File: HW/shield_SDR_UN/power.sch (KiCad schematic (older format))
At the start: 16 parts

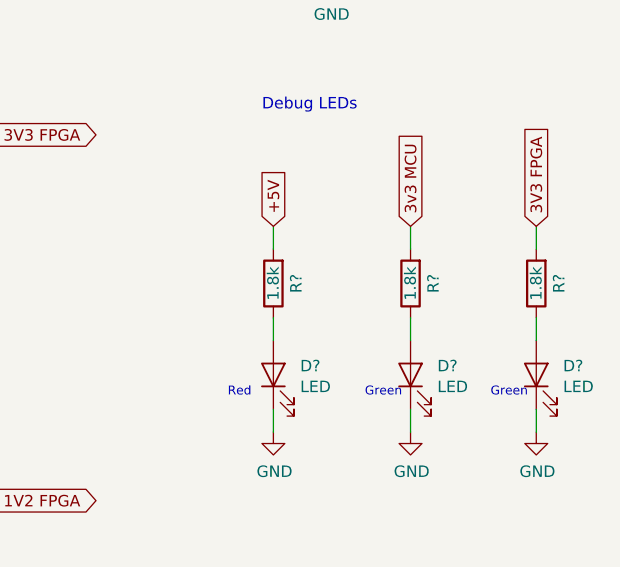
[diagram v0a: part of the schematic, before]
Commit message: Footprints added for C and R
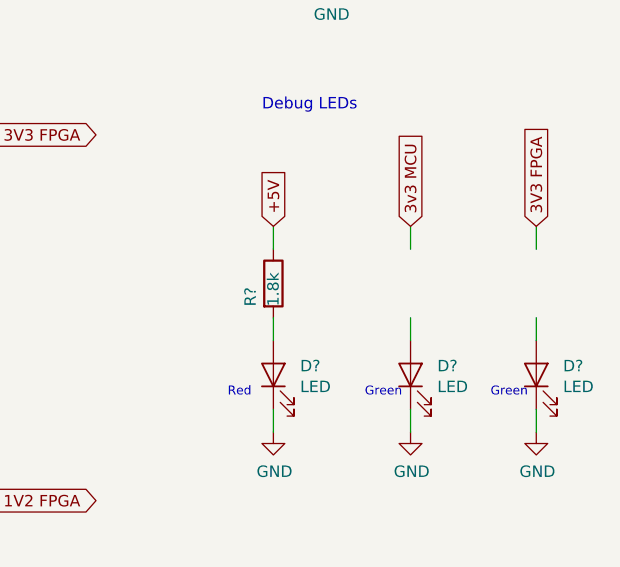
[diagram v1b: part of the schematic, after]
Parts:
- removed C? (x5): 4.7uF, Capacitor_SMD:C_0603_1608Metric_Pad1.05x0.95mm_HandSolder, symbol Device:C
- removed D?: LED, LED_SMD:LED_0805_2012Metric_Pad1.15x1.40mm_HandSolder, symbol Device:LED
- removed R? (x3): 1.8k, Resistor_SMD:R_0603_1608Metric_Pad1.05x0.95mm_HandSolder, symbol Device:R
- added C? (x5): 4.7uF, Capacitor_SMD:C_0603_1608Metric_Pad1.05x0.95mm_HandSolder, symbol Device:C
- added D?: LED, LED_SMD:LED_0805_2012Metric_Pad1.15x1.40mm_HandSolder, symbol Device:LED
- added R?: 1.8k, Resistor_SMD:R_0603_1608Metric_Pad1.05x0.95mm_HandSolder, symbol Device:R
- C?: Digikey (none) -> 1276-1045-1-ND
- D?: footprint LED_SMD:LED_0805_2012Metric_Pad1.15x1.40mm_HandSolder -> LED_SMD:LED_0603_1608Metric_Pad1.05x0.95mm_HandSolder; Digikey (none) -> 160-1469-1-ND
- D?: Digikey (none) -> 160-1468-1-ND
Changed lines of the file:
@@
 Comment4 ""
 $EndDescr
-$Comp
-L Device:C C?
-U 1 1 5CCD952E
-P 1550 3550
-F 0 "C?" H 1665 3596 50  0000 L CNN
-F 1 "4.7uF" H 1665 3505 50  0000 L CNN
-F 2 "Capacitor_SMD:C_0603_1608Metric_Pad1.05x0.95mm_HandSolder" H 1588 3400 50  0001 C CNN
-F 3 "~" H 1550 3550 50  0001 C CNN
-	1    1550 3550
-	1    0    0    -1
-$EndComp
-$Comp
-L Device:C C?
-U 1 1 5CCDBE29
-P 3450 3550
-F 0 "C?" H 3565 3596 50  0000 L CNN
-F 1 "4.7uF" H 3565 3505 50  0000 L CNN
-F 2 "Capacitor_SMD:C_0603_1608Metric_Pad1.05x0.95mm_HandSolder" H 3488 3400 50  0001 C CNN
-F 3 "~" H 3450 3550 50  0001 C CNN
-	1    3450 3550
-	1    0    0    -1
-$EndComp
 Wire Wire Line
 	3850 3300 3450 3300
@@
 Wire Wire Line
 	1550 3850 1550 3700
-$Comp
-L Device:C C?
-U 1 1 5CCEBA00
-P 1550 5150
-F 0 "C?" H 1665 5196 50  0000 L CNN
-F 1 "4.7uF" H 1665 5105 50  0000 L CNN
-F 2 "Capacitor_SMD:C_0603_1608Metric_Pad1.05x0.95mm_HandSolder" H 1588 5000 50  0001 C CNN
-F 3 "~" H 1550 5150 50  0001 C CNN
-	1    1550 5150
-	1    0    0    -1
-$EndComp
 Wire Wire Line
 	3850 4900 3450 4900
@@
 F 1 "4.7uF" H 1665 1955 50  0000 L CNN
 F 2 "Capacitor_SMD:C_0603_1608Metric_Pad1.05x0.95mm_HandSolder" H 1588 1850 50  0001 C CNN
-F 3 "~" H 1550 2000 50  0001 C CNN
+F 3 "www.samsungsem.com/kr/support/product-search/mlcc/CL10A475KQ8NNNC.jsp" H 1550 2000 50  0001 C CNN
+F 4 "1276-1045-1-ND " H 1550 2000 50  0001 C CNN "Digikey"
 	1    1550 2000
-	1    0    0    -1
-$EndComp
-$Comp
-L Device:C C?
-U 1 1 5CD3AA74
-P 3450 2000
-F 0 "C?" H 3565 2046 50  0000 L CNN
-F 1 "4.7uF" H 3565 1955 50  0000 L CNN
-F 2 "Capacitor_SMD:C_0603_1608Metric_Pad1.05x0.95mm_HandSolder" H 3488 1850 50  0001 C CNN
-F 3 "~" H 3450 2000 50  0001 C CNN
-	1    3450 2000
 	1    0    0    -1
 $EndComp
@@
 Text GLabel 1400 3300 0    50   Input ~ 0
 +5V
-$Comp
-L Device:C C?
-U 1 1 5CCEBA0A
-P 3450 5150
-F 0 "C?" H 3565 5196 50  0000 L CNN
-F 1 "4.7uF" H 3565 5105 50  0000 L CNN
-F 2 "Capacitor_SMD:C_0603_1608Metric_Pad1.05x0.95mm_HandSolder" H 3488 5000 50  0001 C CNN
-F 3 "~" H 3450 5150 50  0001 C CNN
-	1    3450 5150
-	1    0    0    -1
-$EndComp
 $Comp
 L power:GND #PWR0187
@@
 Debug LEDs
 $Comp
-L Device:R R?
-U 1 1 5CE70567
-P 5050 3950
-AR Path="/5CC081D2/5CE70567" Ref="R?"  Part="1"
-AR Path="/5CC08321/5CE70567" Ref="R?"  Part="0"
-F 0 "R?" V 4950 3950 50  0000 C CNN
-F 1 "1.8k" V 5050 3950 50  0000 C CNN
-F 2 "Resistor_SMD:R_0603_1608Metric_Pad1.05x0.95mm_HandSolder" V 4980 3950 50  0001 C CNN
-F 3 "~" H 5050 3950 50  0001 C CNN
-	1    5050 3950
-	-1   0    0    1
-$EndComp
-$Comp
 L Device:LED D?
 U 1 1 5CE70571
 P 5050 4350
 AR Path="/5CC081D2/5CE70571" Ref="D?"  Part="1"
-AR Path="/5CC08321/5CE70571" Ref="D?"  Part="0"
+AR Path="/5CC08321/5CE70571" Ref="D?"  Part="1"
 F 0 "D?" V 5089 4233 50  0000 R CNN
 F 1 "LED" V 4998 4233 50  0000 R CNN
-F 2 "LED_SMD:LED_0805_2012Metric_Pad1.15x1.40mm_HandSolder" H 5050 4350 50  0001 C CNN
-F 3 "~" H 5050 4350 50  0001 C CNN
+F 2 "LED_SMD:LED_0603_1608Metric_Pad1.05x0.95mm_HandSolder" H 5050 4350 50  0001 C CNN
+F 3 "optoelectronics.liteon.com/upload/download/DS22-2000-137/LTST-S220KRKT.pdf" H 5050 4350 50  0001 C CNN
+F 4 "160-1469-1-ND" V 5050 4350 50  0001 C CNN "Digikey"
 	1    5050 4350
 	0    -1   -1   0
@@
 Red
 $Comp
-L Device:R R?
-U 1 1 5CE85D9C
-P 5650 3950
-AR Path="/5CC081D2/5CE85D9C" Ref="R?"  Part="1"
-AR Path="/5CC08321/5CE85D9C" Ref="R?"  Part="0"
-F 0 "R?" V 5550 3950 50  0000 C CNN
-F 1 "1.8k" V 5650 3950 50  0000 C CNN
-F 2 "Resistor_SMD:R_0603_1608Metric_Pad1.05x0.95mm_HandSolder" V 5580 3950 50  0001 C CNN
-F 3 "~" H 5650 3950 50  0001 C CNN
-	1    5650 3950
-	-1   0    0    1
-$EndComp
-$Comp
 L Device:LED D?
 U 1 1 5CE85DA6
 P 5650 4350
 AR Path="/5CC081D2/5CE85DA6" Ref="D?"  Part="1"
-AR Path="/5CC08321/5CE85DA6" Ref="D?"  Part="0"
+AR Path="/5CC08321/5CE85DA6" Ref="D?"  Part="1"
 F 0 "D?" V 5689 4233 50  0000 R CNN
 F 1 "LED" V 5598 4233 50  0000 R CNN
 F 2 "LED_SMD:LED_0805_2012Metric_Pad1.15x1.40mm_HandSolder" H 5650 4350 50  0001 C CNN
-F 3 "~" H 5650 4350 50  0001 C CNN
+F 3 "http://optoelectronics.liteon.com/upload/download/DS22-2000-075/LTST-S220KGKT.pdf" H 5650 4350 50  0001 C CNN
+F 4 "160-1468-1-ND" V 5650 4350 50  0001 C CNN "Digikey"
 	1    5650 4350
 	0    -1   -1   0
@@
 Text GLabel 5650 3700 1    50   Input ~ 0
 3v3 MCU
-$Comp
-L Device:R R?
-U 1 1 5CE8EB5C
-P 6200 3950
-AR Path="/5CC081D2/5CE8EB5C" Ref="R?"  Part="1"
-AR Path="/5CC08321/5CE8EB5C" Ref="R?"  Part="0"
-F 0 "R?" V 6100 3950 50  0000 C CNN
-F 1 "1.8k" V 6200 3950 50  0000 C CNN
-F 2 "Resistor_SMD:R_0603_1608Metric_Pad1.05x0.95mm_HandSolder" V 6130 3950 50  0001 C CNN
-F 3 "~" H 6200 3950 50  0001 C CNN
-	1    6200 3950
-	-1   0    0    1
-$EndComp
-$Comp
-L Device:LED D?
-U 1 1 5CE8EB66
-P 6200 4350
-AR Path="/5CC081D2/5CE8EB66" Ref="D?"  Part="1"
-AR Path="/5CC08321/5CE8EB66" Ref="D?"  Part="0"
-F 0 "D?" V 6239 4233 50  0000 R CNN
-F 1 "LED" V 6148 4233 50  0000 R CNN
-F 2 "LED_SMD:LED_0805_2012Metric_Pad1.15x1.40mm_HandSolder" H 6200 4350 50  0001 C CNN
-F 3 "~" H 6200 4350 50  0001 C CNN
-	1    6200 4350
-	0    -1   -1   0
-$EndComp
 Wire Wire Line
 	6200 4600 6200 4500
@@
 	1    0    0    -1
 $EndComp
+$Comp
+L Device:C C?
+U 1 1 5CFF78BF
+P 1550 3550
+F 0 "C?" H 1665 3596 50  0000 L CNN
+F 1 "4.7uF" H 1665 3505 50  0000 L CNN
+F 2 "Capacitor_SMD:C_0603_1608Metric_Pad1.05x0.95mm_HandSolder" H 1588 3400 50  0001 C CNN
+F 3 "www.samsungsem.com/kr/support/product-search/mlcc/CL10A475KQ8NNNC.jsp" H 1550 3550 50  0001 C CNN
+F 4 "1276-1045-1-ND " H 1550 3550 50  0001 C CNN "Digikey"
+	1    1550 3550
+	1    0    0    -1
+$EndComp
+$Comp
+L Device:C C?
+U 1 1 5CFF8436
+P 1550 5150
+F 0 "C?" H 1665 5196 50  0000 L CNN
+F 1 "4.7uF" H 1665 5105 50  0000 L CNN
+F 2 "Capacitor_SMD:C_0603_1608Metric_Pad1.05x0.95mm_HandSolder" H 1588 5000 50  0001 C CNN
+F 3 "www.samsungsem.com/kr/support/product-search/mlcc/CL10A475KQ8NNNC.jsp" H 1550 5150 50  0001 C CNN
+F 4 "1276-1045-1-ND " H 1550 5150 50  0001 C CNN "Digikey"
+	1    1550 5150
+	1    0    0    -1
+$EndComp
+$Comp
+L Device:C C?
+U 1 1 5CFF9817
+P 3450 5150
+F 0 "C?" H 3565 5196 50  0000 L CNN
+F 1 "4.7uF" H 3565 5105 50  0000 L CNN
+F 2 "Capacitor_SMD:C_0603_1608Metric_Pad1.05x0.95mm_HandSolder" H 3488 5000 50  0001 C CNN
+F 3 "www.samsungsem.com/kr/support/product-search/mlcc/CL10A475KQ8NNNC.jsp" H 3450 5150 50  0001 C CNN
+F 4 "1276-1045-1-ND " H 3450 5150 50  0001 C CNN "Digikey"
+	1    3450 5150
+	1    0    0    -1
+$EndComp
+$Comp
+L Device:C C?
+U 1 1 5CFFA74A
+P 3450 3550
+F 0 "C?" H 3565 3596 50  0000 L CNN
+F 1 "4.7uF" H 3565 3505 50  0000 L CNN
+F 2 "Capacitor_SMD:C_0603_1608Metric_Pad1.05x0.95mm_HandSolder" H 3488 3400 50  0001 C CNN
+F 3 "www.samsungsem.com/kr/support/product-search/mlcc/CL10A475KQ8NNNC.jsp" H 3450 3550 50  0001 C CNN
+F 4 "1276-1045-1-ND " H 3450 3550 50  0001 C CNN "Digikey"
+	1    3450 3550
+	1    0    0    -1
+$EndComp
+$Comp
+L Device:C C?
+U 1 1 5CFFC6D1
+P 3450 2000
+F 0 "C?" H 3565 2046 50  0000 L CNN
+F 1 "4.7uF" H 3565 1955 50  0000 L CNN
+F 2 "Capacitor_SMD:C_0603_1608Metric_Pad1.05x0.95mm_HandSolder" H 3488 1850 50  0001 C CNN
+F 3 "www.samsungsem.com/kr/support/product-search/mlcc/CL10A475KQ8NNNC.jsp" H 3450 2000 50  0001 C CNN
+F 4 "1276-1045-1-ND " H 3450 2000 50  0001 C CNN "Digikey"
+	1    3450 2000
+	1    0    0    -1
+$EndComp
+$Comp
+L Device:R R?
+U 1 1 5D0251D4
+P 5050 3950
+F 0 "R?" V 4950 3850 50  0000 L CNN
+F 1 "1.8k" V 5050 3850 50  0000 L CNN
+F 2 "Resistor_SMD:R_0603_1608Metric_Pad1.05x0.95mm_HandSolder" V 4980 3950 50  0001 C CNN
+F 3 "http://www.yageo.com/documents/recent/PYu-RC_Group_51_RoHS_L_10.pdf" H 5050 3950 50  0001 C CNN
+F 4 "311-1.8KGRTR-ND" V 5050 3950 50  0001 C CNN "Digikey"
+	1    5050 3950
+	1    0    0    -1
+$EndComp
+$Comp
+L Device:LED D?
+U 1 1 5D05C7DE
+P 6200 4350
+AR Path="/5CC081D2/5D05C7DE" Ref="D?"  Part="1"
+AR Path="/5CC08321/5D05C7DE" Ref="D?"  Part="1"
+F 0 "D?" V 6239 4233 50  0000 R CNN
+F 1 "LED" V 6148 4233 50  0000 R CNN
+F 2 "LED_SMD:LED_0805_2012Metric_Pad1.15x1.40mm_HandSolder" H 6200 4350 50  0001 C CNN
+F 3 "http://optoelectronics.liteon.com/upload/download/DS22-2000-075/LTST-S220KGKT.pdf" H 6200 4350 50  0001 C CNN
+F 4 "160-1468-1-ND" V 6200 4350 50  0001 C CNN "Digikey"
+	1    6200 4350
+	0    -1   -1   0
+$EndComp
 $EndSCHEMATC

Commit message: Footprints updated
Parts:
- removed R?: 1.8k, Resistor_SMD:R_0603_1608Metric_Pad1.05x0.95mm_HandSolder, symbol Device:R
- added R? (x2): 470, Resistor_SMD:R_0603_1608Metric_Pad1.05x0.95mm_HandSolder, symbol Device:R
- added R?: 1.8k, Resistor_SMD:R_0603_1608Metric_Pad1.05x0.95mm_HandSolder, symbol Device:R
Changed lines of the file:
@@
-$EndComp
-$Comp
-L Device:R R?
-U 1 1 5D0251D4
-P 5050 3950
-F 0 "R?" V 4950 3850 50  0000 L CNN
-F 1 "1.8k" V 5050 3850 50  0000 L CNN
-F 2 "Resistor_SMD:R_0603_1608Metric_Pad1.05x0.95mm_HandSolder" V 4980 3950 50  0001 C CNN
-F 3 "http://www.yageo.com/documents/recent/PYu-RC_Group_51_RoHS_L_10.pdf" H 5050 3950 50  0001 C CNN
-F 4 "311-1.8KGRTR-ND" V 5050 3950 50  0001 C CNN "Digikey"
-	1    5050 3950
-	1    0    0    -1
 $EndComp
 $Comp
@@
 	0    -1   -1   0
 $EndComp
+$Comp
+L Device:R R?
+U 1 1 5CEB8F9A
+P 5650 3950
+F 0 "R?" H 5700 4000 50  0000 L CNN
+F 1 "470" V 5650 3850 50  0000 L CNN
+F 2 "Resistor_SMD:R_0603_1608Metric_Pad1.05x0.95mm_HandSolder" V 5580 3950 50  0001 C CNN
+F 3 "http://www.yageo.com/documents/recent/PYu-RC_Group_51_RoHS_L_10.pdf" H 5650 3950 50  0001 C CNN
+F 4 "311-470GRCT-ND" V 5650 3950 50  0001 C CNN "Digikey"
+	1    5650 3950
+	1    0    0    -1
+$EndComp
+$Comp
+L Device:R R?
+U 1 1 5CEB98F9
+P 6200 3950
+F 0 "R?" H 6250 4000 50  0000 L CNN
+F 1 "470" V 6200 3850 50  0000 L CNN
+F 2 "Resistor_SMD:R_0603_1608Metric_Pad1.05x0.95mm_HandSolder" V 6130 3950 50  0001 C CNN
+F 3 "http://www.yageo.com/documents/recent/PYu-RC_Group_51_RoHS_L_10.pdf" H 6200 3950 50  0001 C CNN
+F 4 "311-470GRCT-ND" V 6200 3950 50  0001 C CNN "Digikey"
+	1    6200 3950
+	1    0    0    -1
+$EndComp
+$Comp
+L Device:R R?
+U 1 1 5CEE7448
+P 5050 3950
+F 0 "R?" H 5100 4000 50  0000 L CNN
+F 1 "1.8k" V 5050 3850 50  0000 L CNN
+F 2 "Resistor_SMD:R_0603_1608Metric_Pad1.05x0.95mm_HandSolder" V 4980 3950 50  0001 C CNN
+F 3 "http://www.yageo.com/documents/recent/PYu-RC_Group_51_RoHS_L_10.pdf" H 5050 3950 50  0001 C CNN
+F 4 "311-1.8KGRTR-ND" V 5050 3950 50  0001 C CNN "Digikey"
+	1    5050 3950
+	1    0    0    -1
+$EndComp
 $EndSCHEMATC

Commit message: RF-Front-end connections
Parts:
- J?: footprint Connector_USB:USB_Micro-B_GCT_USB3076-30-A -> lib:USB_Micro_B_Female_10118194-0001LF; Digikey (none) -> 609-4618-1-ND
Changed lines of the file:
@@
 F 0 "J?" H 5407 2417 50  0000 C CNN
 F 1 "USB_B_Micro" H 5407 2326 50  0000 C CNN
-F 2 "Connector_USB:USB_Micro-B_GCT_USB3076-30-A" H 5500 1900 50  0001 C CNN
-F 3 "~" H 5500 1900 50  0001 C CNN
+F 2 "lib:USB_Micro_B_Female_10118194-0001LF" H 5500 1900 50  0001 C CNN
+F 3 "https://cdn.amphenol-icc.com/media/wysiwyg/files/documentation/datasheet/inputoutput/io_usb_micro.pdf" H 5500 1900 50  0001 C CNN
+F 4 "609-4618-1-ND" H 5350 1950 50  0001 C CNN "Digikey"
 	1    5350 1950
 	1    0    0    -1

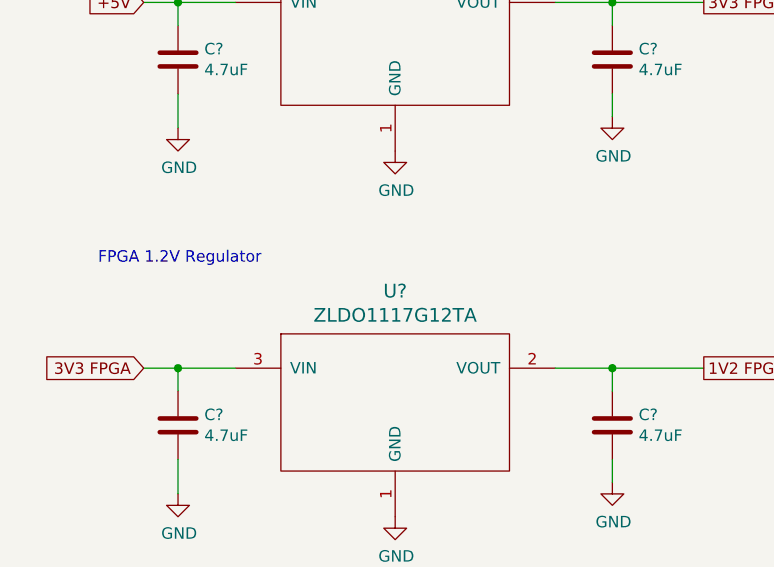
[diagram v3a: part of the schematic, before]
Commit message: JTAG routed
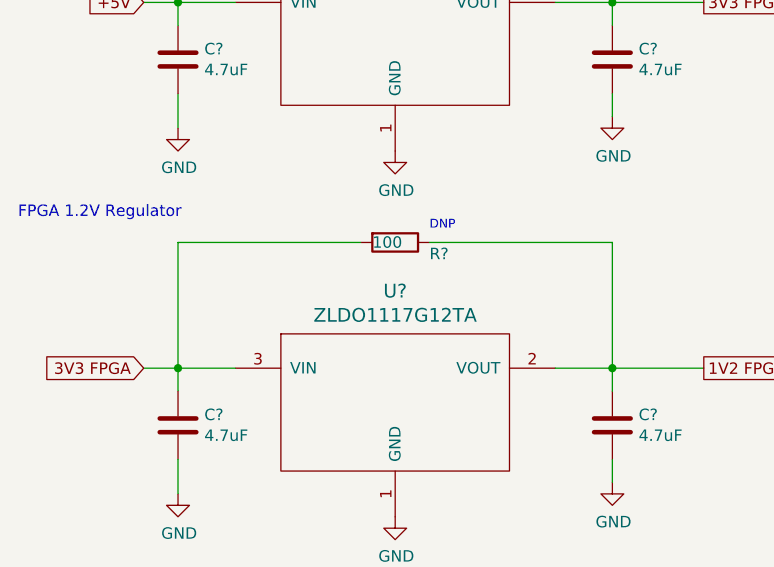
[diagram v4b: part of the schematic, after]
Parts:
- added R?: 100, Resistor_SMD:R_0603_1608Metric_Pad1.05x0.95mm_HandSolder, symbol Device:R
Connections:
- net 1V2 FPGA: now also R?.1
- net 3V3 FPGA: now also R?.2
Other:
- note added: "DNP"
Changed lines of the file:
@@
 Text Notes 1200 2900 0    50   ~ 0
 FPGA 3.3V Regulator
-Text Notes 1200 4450 0    50   ~ 0
+Text Notes 850  4250 0    50   ~ 0
 FPGA 1.2V Regulator
 Text Notes 5000 1300 0    50   ~ 0
@@
 	1    0    0    -1
 $EndComp
+$Comp
+L Device:R R?
+U 1 1 5D09DB9D
+P 2500 4350
+F 0 "R?" V 2550 4500 50  0000 L CNN
+F 1 "100" V 2500 4250 50  0000 L CNN
+F 2 "Resistor_SMD:R_0603_1608Metric_Pad1.05x0.95mm_HandSolder" V 2430 4350 50  0001 C CNN
+F 3 "http://www.yageo.com/documents/recent/PYu-RC_Group_51_RoHS_L_10.pdf" H 2500 4350 50  0001 C CNN
+F 4 "311-470GRCT-ND" V 2500 4350 50  0001 C CNN "Digikey"
+	1    2500 4350
+	0    1    1    0
+$EndComp
+Wire Wire Line
+	2650 4350 3450 4350
+Wire Wire Line
+	3450 4350 3450 4900
+Wire Wire Line
+	2350 4350 1550 4350
+Wire Wire Line
+	1550 4350 1550 4900
+Text Notes 2650 4300 0    39   ~ 0
+DNP
 $EndSCHEMATC

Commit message: i2c_complete
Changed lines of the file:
@@
 $Comp
 L Connector:USB_B_Micro J?
-U 1 1 5D009192
+U 0 0 5D009192
 P 5350 1950
 F 0 "J?" H 5407 2417 50  0000 C CNN
@@
 F 3 "https://cdn.amphenol-icc.com/media/wysiwyg/files/documentation/datasheet/inputoutput/io_usb_micro.pdf" H 5500 1900 50  0001 C CNN
 F 4 "609-4618-1-ND" H 5350 1950 50  0001 C CNN "Digikey"
-	1    5350 1950
+	0    5350 1950
 	1    0    0    -1
 $EndComp

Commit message: Schematic finished
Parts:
- removed C? (x6): 4.7uF, Capacitor_SMD:C_0603_1608Metric_Pad1.05x0.95mm_HandSolder, symbol Device:C
- added C113, C114, C115, C119, C120, C121: 22uF, Resistor_SMD:R_0603_1608Metric_Pad1.05x0.95mm_HandSolder, symbol Device:C
- added C116, C117, C118: 100nF, Capacitor_SMD:C_0603_1608Metric_Pad1.05x0.95mm_HandSolder, symbol Device:C
- R58: renamed from R?; Digikey 311-470GRCT-ND -> 311-100HRCT-ND
- gave numbers to parts that had none: 10
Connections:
- wire segments 43 -> 52

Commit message: organizacion PCB
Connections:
- net 3v3 MCU renamed 3V3 MCU
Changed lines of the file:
@@
 	1    0    0    -1
 $EndComp
-Text GLabel 4175 1750 2    50   Output ~ 0
-3v3 MCU
 Text GLabel 4200 3300 2    50   Output ~ 0
 3V3 FPGA
@@
 Wire Wire Line
 	5650 4200 5650 4100
-Wire Wire Line
-	5650 3800 5650 3700
 $Comp
 L power:GND #PWR0140
@@
 Text Notes 5450 4450 0    39   ~ 0
 Green\n
-Text GLabel 5650 3700 1    50   Input ~ 0
-3v3 MCU
 Wire Wire Line
 	6200 4600 6200 4500
@@
 Wire Wire Line
 	3900 1850 3900 1750
-Connection ~ 3900 1750
-Wire Wire Line
-	3900 1750 4175 1750
 Wire Wire Line
 	3875 3400 3875 3300
@@
 	1    0    0    -1
 $EndComp
+Text GLabel 4150 1750 2    50   Input ~ 0
+3V3 MCU
+Wire Wire Line
+	4150 1750 3900 1750
+Connection ~ 3900 1750
+Text GLabel 5650 3650 1    50   Input ~ 0
+3V3 MCU
+Wire Wire Line
+	5650 3800 5650 3650
 $EndSCHEMATC

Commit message: PCB route V1
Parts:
- D7: footprint LED_SMD:LED_0603_1608Metric_Pad1.05x0.95mm_HandSolder -> LED_SMD:LED_0805_2012Metric_Pad1.15x1.40mm_HandSolder
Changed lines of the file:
@@
 $Comp
 L Device:LED D?
-U 1 1 5CE70571
+U 1 0 5CE70571
 P 5050 4350
 AR Path="/5CC081D2/5CE70571" Ref="D?"  Part="1"
@@
 F 0 "D7" V 5089 4233 50  0000 R CNN
 F 1 "LED" V 4998 4233 50  0000 R CNN
-F 2 "LED_SMD:LED_0603_1608Metric_Pad1.05x0.95mm_HandSolder" H 5050 4350 50  0001 C CNN
+F 2 "LED_SMD:LED_0805_2012Metric_Pad1.15x1.40mm_HandSolder" H 5050 4350 50  0001 C CNN
 F 3 "optoelectronics.liteon.com/upload/download/DS22-2000-137/LTST-S220KRKT.pdf" H 5050 4350 50  0001 C CNN
 F 4 "160-1469-1-ND" V 5050 4350 50  0001 C CNN "Digikey"
